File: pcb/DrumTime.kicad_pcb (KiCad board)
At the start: 2 copper layers, 100 x 100 mm, 132 parts, among them CN1 Motor, CN2 Motor, CN3 Motor, CN4 Motor, J1 EN, J2 Boot, J3 Debug, J4 LED_Conn, J5 LED_Conn, J6 Hall, J7 Hall, J8 Hall, J9 Hall, U1 ME6210A33PG, U10 TMC2209-LA, U12 TMC2209-LA, U2 ESP32-S3-WROOM-1-N8, U3 TJ-S1608SW6TDSLCCYRGB-A5, U4 IS31FL3236A-QFLS2-TR, U6 TMC2209-LA, U8 TMC2209-LA

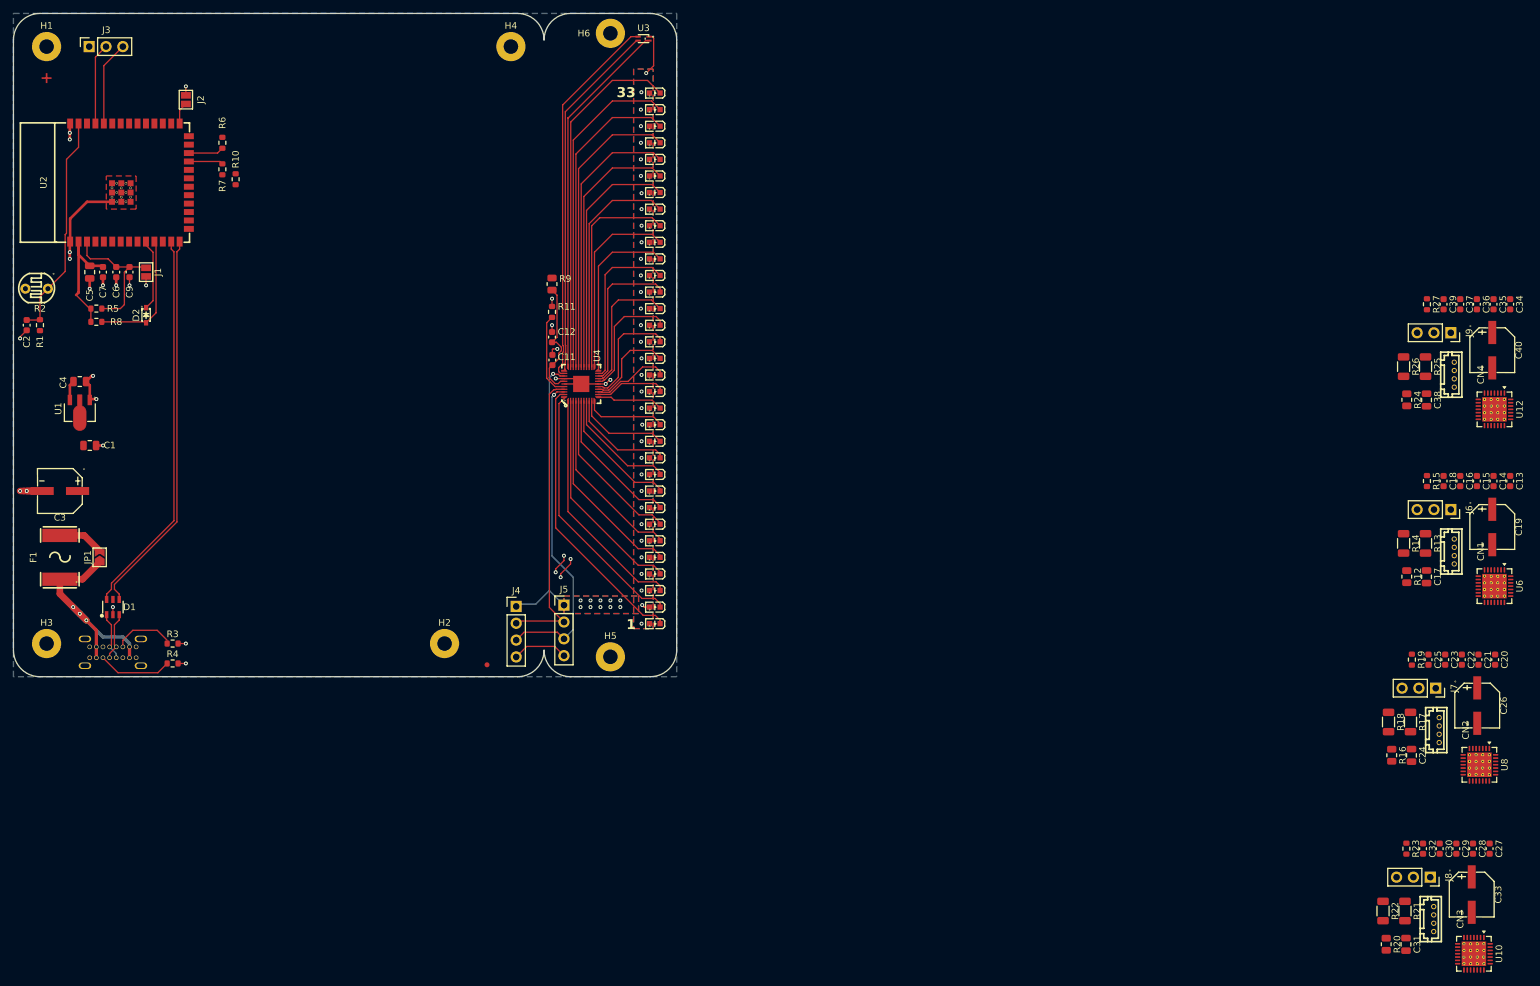
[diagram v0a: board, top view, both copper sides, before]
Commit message: feat(pcb): layout motor drivers and route internally
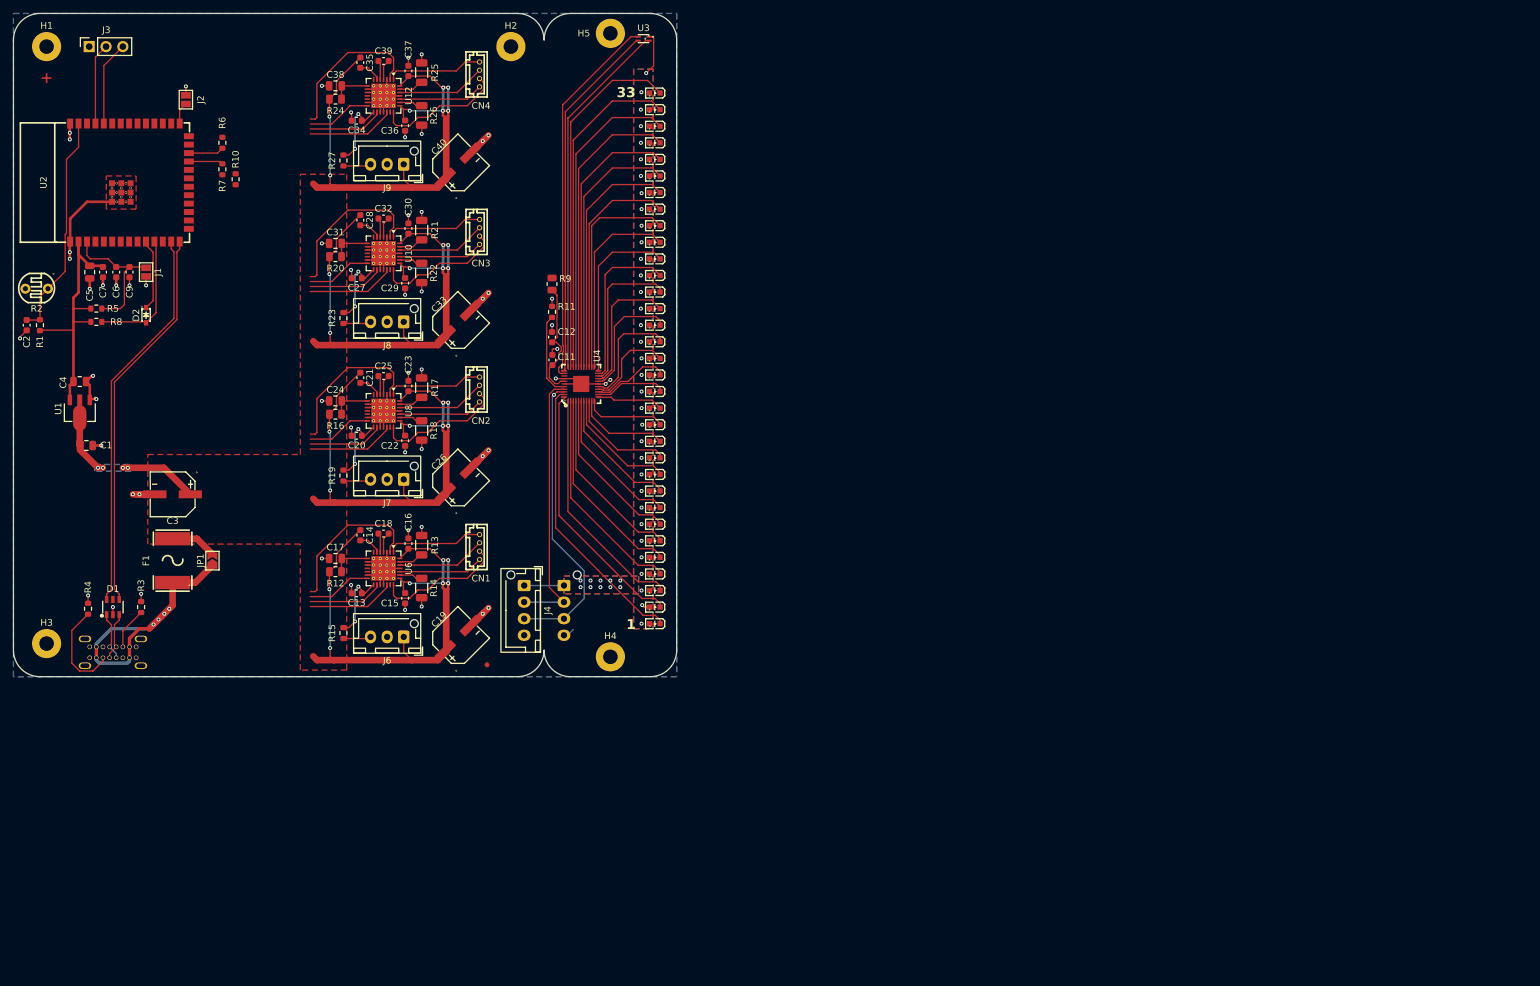
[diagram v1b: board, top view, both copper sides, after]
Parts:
- removed the H2 at (80.0, 110.0)
- J4: footprint Connector_PinHeader_2.54mm:PinHeader_1x04_P2.54mm_Vertical -> Connector_JST:JST_XH_B4B-XH-AM_1x04_P2.50mm_Vertical
- J5: footprint Connector_PinHeader_2.54mm:PinHeader_1x04_P2.54mm_Vertical -> Connector_JST:JST_XH_B4B-XH-AM_1x04_P2.50mm_Vertical; moved to B.Cu
- J6, J7, J8, J9: footprint Connector_PinSocket_2.54mm:PinSocket_1x03_P2.54mm_Vertical -> Connector_JST:JST_XH_B3B-XH-AM_1x03_P2.50mm_Vertical
- moved U10 195.4 mm to (70.8, 51.2)
- moved C31 192.9 mm to (63.5, 49.7), turned to 0 degrees
- moved C28 192.7 mm to (67.3, 46.2)
- moved C27 191.2 mm to (66.8, 54.9), turned to 180 degrees
- moved R20 189.3 mm to (63.5, 51.7), turned to 0 degrees
- moved C32 183.3 mm to (70.8, 45.9), turned to 180 degrees
- moved C30 181.4 mm to (74.5, 47.4), turned to 90 degrees
- moved R21 180.3 mm to (76.5, 47.7), turned to 90 degrees
- moved C29 180.0 mm to (74.0, 55.7)
- moved R23 179.1 mm to (64.8, 60.9)
- moved CN3 177.3 mm to (85.3, 47.9)
- moved C34 176.1 mm to (66.8, 31.2), turned to 180 degrees
- moved J8 176.0 mm to (73.8, 61.5), turned to 180 degrees
- moved C33 175.5 mm to (82.0, 61.7), turned to 45 degrees
- moved C20 174.9 mm to (66.8, 78.7), turned to 180 degrees
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- renumbered H4 to H2, H5 to H4, H6 to H5
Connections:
- U2 pad : GND -> (no net)
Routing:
- net +5V: track 58.7 -> 377.2 mm, vias 45 -> 76
- net GND: track 71.2 -> 171.8 mm, vias 29 -> 57
- net /m_enn: track 0.00 -> 94.1 mm
- net +3V3: track 22.7 -> 85.7 mm, vias 0 -> 8
- net /m_uart: track 19.7 -> 58.7 mm
- net /Motor2/A-: track 0.00 -> 19.6 mm
- net /Motor3/A-: track 0.00 -> 19.6 mm
- net /Motor1/A-: track 0.00 -> 19.6 mm
- net /Motor/A-: track 0.00 -> 19.6 mm
- net /Motor2/B-: track 0.00 -> 14.6 mm
- net /Motor1/B-: track 0.00 -> 14.6 mm
- net /Motor/B-: track 0.00 -> 14.6 mm
- net /Motor3/B-: track 0.00 -> 14.6 mm
- net /Motor2/B+: track 0.00 -> 13.4 mm
- net /Motor1/B+: track 0.00 -> 13.4 mm
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
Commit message: feat(pcb): finish initial routing and layouting
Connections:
- C11 pad 1: Net-(U4-VCC) -> /SDB
- C12 pad 1: Net-(U4-VCC) -> /SDB
- R9 pad 2: Net-(U4-VCC) -> /SDB
- U2 pad : (no net) -> GND
- U2 pad 12: /m2_step -> /m2_hall
- U2 pad 17: /m2_hall -> /m2_dir
- U2 pad 18: /m2_dir -> /m2_step
- U2 pad 19: /m3_step -> /m3_hall
- U2 pad 20: /m3_hall -> /m3_dir
- U2 pad 21: /m3_dir -> /m3_step
- U2 pad 4: /m0_step -> /m0_hall
- U2 pad 5: /m0_hall -> /m0_dir
- U2 pad 6: /m0_dir -> /m0_step
- U2 pad 7: /m1_step -> /m1_hall
- U2 pad 8: /m1_hall -> /m1_dir
- U2 pad 9: /m1_dir -> /m1_step
- U4 pad 36: +5V -> /SDB
- U4 pad 38: Net-(U4-VCC) -> /SDB
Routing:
- net /SDA: track 46.2 -> 178.5 mm
- net /m_uart: track 58.7 -> 186.5 mm, vias 0 -> 13
- net +3V3: track 85.7 -> 205.3 mm, vias 8 -> 12
- net /SCL: track 50.3 -> 160.7 mm
- net /m0_hall: track 4.31 -> 81.4 mm, vias 0 -> 8
- net /m_enn: track 94.1 -> 169.4 mm, vias 0 -> 8
- net /m0_dir: track 13.2 -> 82.1 mm, vias 0 -> 8
- net /m0_step: track 11.3 -> 78.0 mm, vias 0 -> 8
- net /m1_hall: track 4.31 -> 62.9 mm, vias 0 -> 5
- net /m1_dir: track 13.2 -> 63.3 mm, vias 0 -> 4
- net /m1_step: track 11.3 -> 60.5 mm, vias 0 -> 6
- net /m2_hall: track 4.31 -> 40.5 mm, vias 0 -> 4
- net GND: track 171.8 -> 202.2 mm, vias 57 -> 83
- net /m2_dir: track 13.2 -> 38.8 mm, vias 0 -> 4
- net /m3_hall: track 4.31 -> 29.4 mm, vias 0 -> 2
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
